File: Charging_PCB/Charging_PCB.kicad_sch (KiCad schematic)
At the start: 9 parts, among them K3 BMS_Relay, K4 IMD_Relay, Q1 PMOS, Q2 PMOS, SW1 Charger Shutdown Button

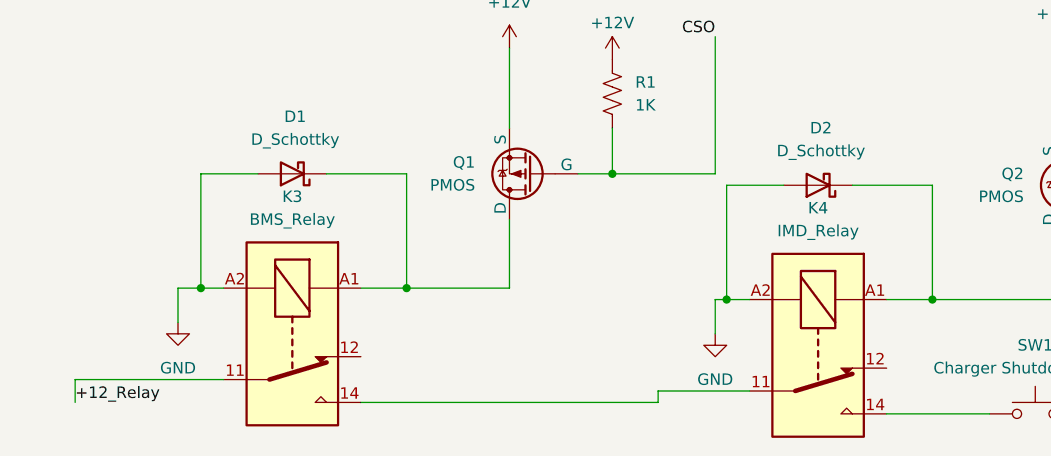
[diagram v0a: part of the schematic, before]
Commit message: Updated Charging PCB Layout
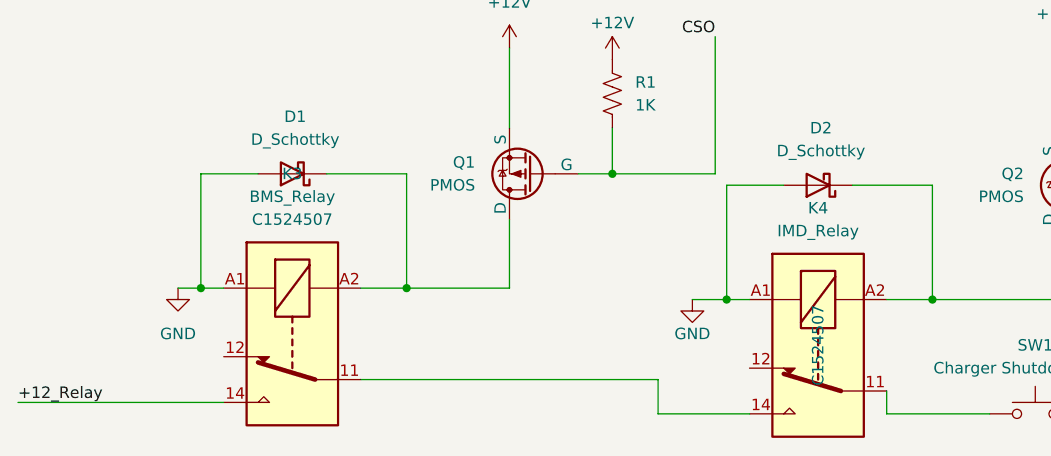
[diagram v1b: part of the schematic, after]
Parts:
- K3, K4: JLC# (none) -> C1524507
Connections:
- net +12_Relay: now also K3.14; no longer K3.11
- net GND: now also K3.A1, K4.A1; no longer K3.A2, K4.A2
- net at D1.1 (K), Q1.1 (D): now also K3.A2; no longer K3.A1
- net at SW1.1 (A), SW1.2 (A): now also K4.11; no longer K4.14
- net at D2.1 (K), Q2.1 (D): now also K4.A2; no longer K4.A1
- new net: K3.11, K4.14
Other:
- moved on the sheet: K3, K4
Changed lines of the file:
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@@
 	(wire
 		(pts
-			(xy 111.76 58.42) (xy 111.76 62.23)
+			(xy 130.81 68.58) (xy 130.81 71.12)
 		)
 		(stroke
@@
 	(wire
 		(pts
-			(xy 113.03 58.42) (xy 111.76 58.42)
+			(xy 113.03 58.42) (xy 109.22 58.42)
 		)
 		(stroke
@@
 	(wire
 		(pts
-			(xy 105.41 68.58) (xy 115.57 68.58)
+			(xy 105.41 71.12) (xy 115.57 71.12)
 		)
 		(stroke
@@
 	(wire
 		(pts
-			(xy 57.15 67.31) (xy 40.64 67.31)
+			(xy 34.29 69.85) (xy 57.15 69.85)
 		)
 		(stroke
@@
 	(wire
 		(pts
-			(xy 52.07 57.15) (xy 52.07 60.96)
-		)
-		(stroke
-			(width 0)
-			(type default)
-		)
-	)
-	(wire
-		(pts
 			(xy 88.9 57.15) (xy 77.47 57.15)
 		)
@@
 	(wire
 		(pts
-			(xy 72.39 69.85) (xy 105.41 69.85)
+			(xy 72.39 67.31) (xy 105.41 67.31)
 		)
 		(stroke
@@
 	(wire
 		(pts
-			(xy 40.64 67.31) (xy 40.64 69.85)
-		)
-		(stroke
-			(width 0)
-			(type default)
-		)
-	)
-	(wire
-		(pts
 			(xy 111.76 44.45) (xy 100.33 44.45)
 		)
@@
 	(wire
 		(pts
-			(xy 105.41 69.85) (xy 105.41 68.58)
+			(xy 105.41 67.31) (xy 105.41 71.12)
 		)
 		(stroke
@@
 	)
 	(label "+12_Relay"
-		(at 40.64 69.85 0)
+		(at 34.29 69.85 0)
 		(effects
 			(font
@@
 			)
 		)
+		(property "JLC#" ""
+			(at 91.44 44.45 0)
+			(effects
+				(font
+					(size 1.27 1.27)
+				)
+			)
+		)
 		(pin "2"
 		)
@@
 			)
 		)
+		(property "JLC#" ""
+			(at 147.32 71.12 0)
+			(effects
+				(font
+					(size 1.27 1.27)
+				)
+			)
+		)
 		(pin "2"
 		)
@@
 			)
 		)
+		(property "JLC#" ""
+			(at 152.4 45.72 0)
+			(effects
+				(font
+					(size 1.27 1.27)
+				)
+			)
+		)
 		(pin "2"
 		)
@@
 	(symbol
 		(lib_id "power:GND")
-		(at 52.07 60.96 0)
+		(at 52.07 57.15 0)
 		(unit 1)
 		(exclude_from_sim no)
@@
 		(fields_autoplaced yes)
 		(property "Reference" "#PWR04"
-			(at 52.07 67.31 0)
+			(at 52.07 63.5 0)
 			(effects
 				(font
@@
 		)
 		(property "Value" "GND"
-			(at 52.07 66.04 0)
+			(at 52.07 62.23 0)
 			(effects
 				(font
@@
 		)
 		(property "Footprint" ""
-			(at 52.07 60.96 0)
+			(at 52.07 57.15 0)
 			(effects
 				(font
@@
 		)
 		(property "Datasheet" ""
-			(at 52.07 60.96 0)
+			(at 52.07 57.15 0)
 			(effects
 				(font
@@
 		)
 		(property "Description" "Power symbol creates a global label with name \"GND\" , ground"
-			(at 52.07 60.96 0)
+			(at 52.07 57.15 0)
 			(effects
 				(font
@@
 			)
 		)
+		(property "JLC#" ""
+			(at 64.77 44.45 0)
+			(effects
+				(font
+					(size 1.27 1.27)
+				)
+			)
+		)
 		(pin "2"
 		)
@@
 	(symbol
 		(lib_id "Relay:G2RL-1")
-		(at 64.77 62.23 270)
+		(at 64.77 62.23 90)
+		(mirror x)
 		(unit 1)
 		(exclude_from_sim no)
@@
 		(on_board yes)
 		(dnp no)
-		(fields_autoplaced yes)
 		(property "Reference" "K3"
+			(at 64.77 44.45 90)
+			(effects
+				(font
+					(size 1.27 1.27)
+				)
+			)
+		)
+		(property "Value" "BMS_Relay"
 			(at 64.77 46.99 90)
 			(effects
@@
 			)
 		)
-		(property "Value" "BMS_Relay"
-			(at 64.77 49.53 90)
-			(effects
-				(font
-					(size 1.27 1.27)
-				)
-			)
-		)
 		(property "Footprint" "Relay_THT:Relay_SPDT_Omron_G2RL-1"
-			(at 63.5 73.66 0)
+			(at 66.04 73.66 0)
 			(effects
 				(font
@@
 				)
 				(hide yes)
+			)
+		)
+		(property "JLC#" "C1524507"
+			(at 64.77 49.53 90)
+			(effects
+				(font
+					(size 1.27 1.27)
+				)
 			)
 		)
@@
 	(symbol
 		(lib_id "power:GND")
-		(at 111.76 62.23 0)
+		(at 109.22 58.42 0)
 		(unit 1)
 		(exclude_from_sim no)
@@
 		(on_board yes)
 		(dnp no)
-		(fields_autoplaced yes)
 		(property "Reference" "#PWR05"
-			(at 111.76 68.58 0)
+			(at 109.22 64.77 0)
 			(effects
 				(font
@@
 		)
 		(property "Value" "GND"
-			(at 111.76 67.31 0)
+			(at 109.22 62.23 0)
 			(effects
 				(font
@@
 		)
 		(property "Footprint" ""
-			(at 111.76 62.23 0)
+			(at 109.22 58.42 0)
 			(effects
 				(font
@@
 		)
 		(property "Datasheet" ""
-			(at 111.76 62.23 0)
+			(at 109.22 58.42 0)
 			(effects
 				(font
@@
 		)
 		(property "Description" "Power symbol creates a global label with name \"GND\" , ground"
-			(at 111.76 62.23 0)
+			(at 109.22 58.42 0)
 			(effects
 				(font
@@
 	(symbol
 		(lib_id "Relay:G2RL-1")
-		(at 123.19 63.5 270)
+		(at 123.19 63.5 90)
+		(mirror x)
 		(unit 1)
 		(exclude_from_sim no)
@@
 		(on_board yes)
 		(dnp no)
-		(fields_autoplaced yes)
 		(property "Reference" "K4"
 			(at 123.19 48.26 90)
@@
 		)
 		(property "Footprint" "Relay_THT:Relay_SPDT_Omron_G2RL-1"
-			(at 121.92 74.93 0)
+			(at 124.46 74.93 0)
 			(effects
 				(font
@@
 				)
 				(hide yes)
+			)
+		)
+		(property "JLC#" "C1524507"
+			(at 123.19 63.5 0)
+			(effects
+				(font
+					(size 1.27 1.27)
+				)
 			)
 		)
@@
 			)
 		)
+		(property "JLC#" ""
+			(at 100.33 35.56 0)
+			(effects
+				(font
+					(size 1.27 1.27)
+				)
+			)
+		)
 		(pin "1"
 		)
@@
 			)
 		)
+		(property "JLC#" ""
+			(at 160.02 52.07 0)
+			(effects
+				(font
+					(size 1.27 1.27)
+				)
+			)
+		)
 		(pin "1"
 		)
@@
 			)
 		)
+		(property "JLC#" ""
+			(at 123.19 45.72 0)
+			(effects
+				(font
+					(size 1.27 1.27)
+				)
+			)
+		)

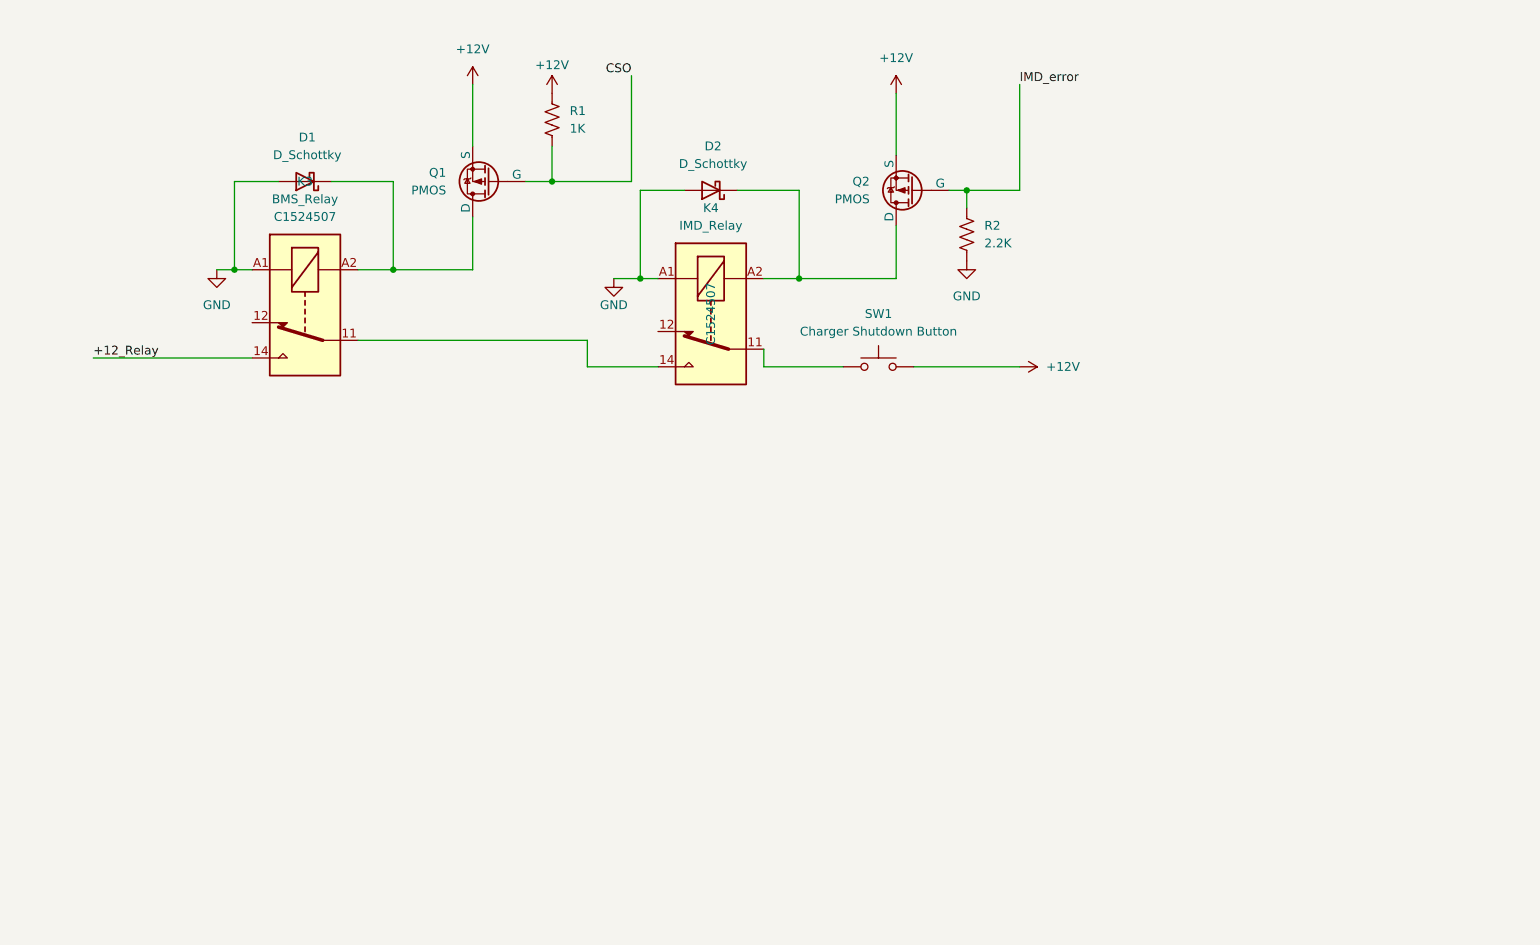
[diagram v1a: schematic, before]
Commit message: unfinished connector addition to schematic
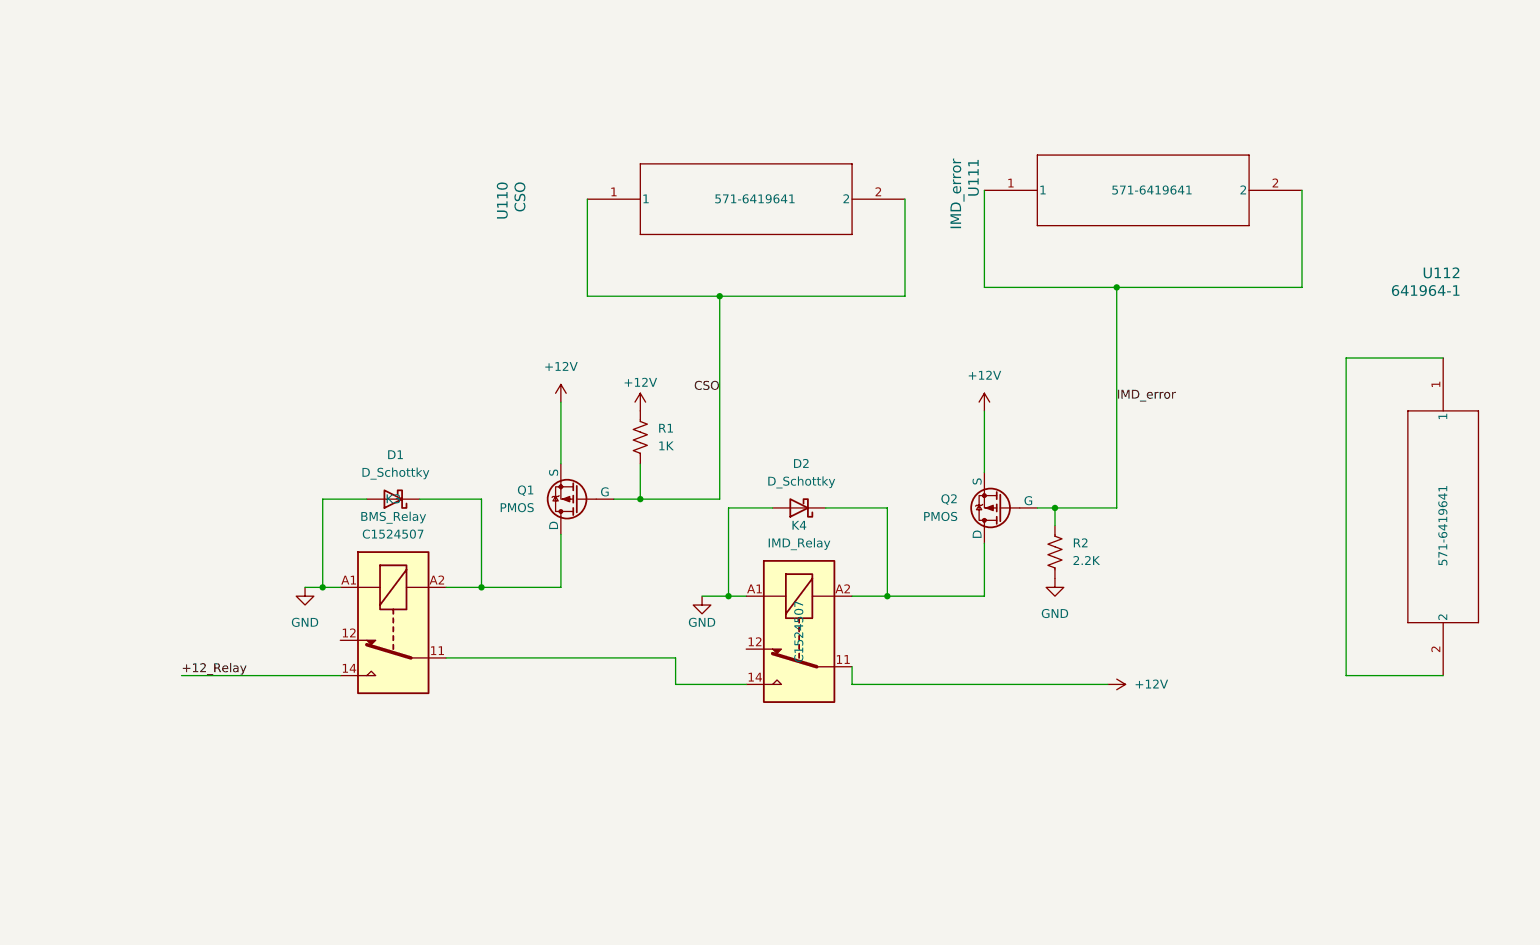
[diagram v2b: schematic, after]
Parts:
- removed SW1: Charger Shutdown Button, symbol Switch:SW_MEC_5G
- added U110: CSO, 641964-1:TE_641964-1, symbol CONNECTOR:641964-1
- added U111: IMD_error, 641964-1:TE_641964-1, symbol CONNECTOR:641964-1
- added U112: 641964-1, 641964-1:TE_641964-1, symbol CONNECTOR:641964-1
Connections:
- net +12V: now also K4.11
- net CSO: now also U110.1, U110.2
- net IMD_error: now also U111.1, U111.2
- new net: U112.1, U112.2
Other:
- moved on the sheet: D1, D2, K3, K4, Q1, Q2, R1, R2

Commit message: added connectors, relay traces, mounting holes, labels
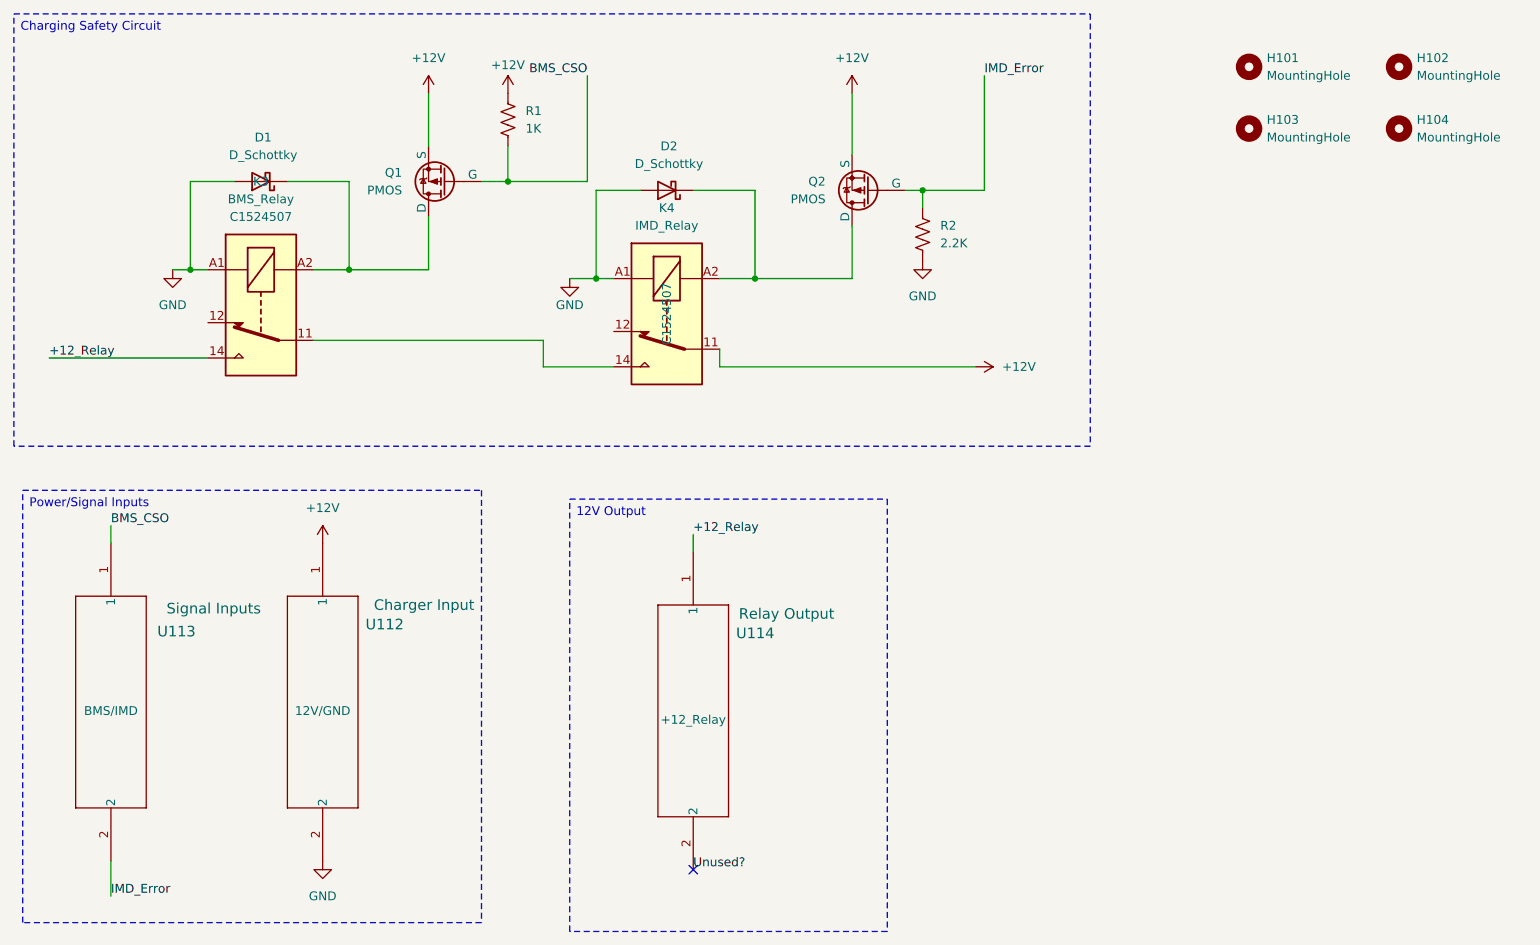
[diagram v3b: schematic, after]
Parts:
- removed U110: CSO, 641964-1:TE_641964-1, symbol CONNECTOR:641964-1
- removed U111: IMD_error, 641964-1:TE_641964-1, symbol CONNECTOR:641964-1
- added H101, H102, H103, H104: MountingHole, MountingHole:MountingHole_3.2mm_M3, symbol Mechanical:MountingHole
- added U113: Signal Inputs, 641964-1:TE_641964-1, symbol CONNECTOR:641964-1
- added U114: Relay Output, 641964-1:TE_641964-1, symbol CONNECTOR:641964-1
- U112: value 641964-1 -> Charger Input; MOUSER 571-6419641 -> 12V/GND
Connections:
- net +12V: now also U112.1
- net +12_Relay: now also U114.1
- net GND: now also U112.2
- net CSO renamed BMS_CSO
- net BMS_CSO: now also U113.1
- net IMD_error renamed IMD_Error
- net IMD_Error: now also U113.2
- new net Unused?: U114.2
- no-connect marks 0 -> 1
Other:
- moved on the sheet: D1, D2, K3, K4, Q1, Q2, R1, R2, U112
